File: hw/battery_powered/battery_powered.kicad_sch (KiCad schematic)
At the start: 11 parts, among them SW101 SKRPABE010, SW102 SKRPABE010, U101 RP2040, U102 OSL10564-IB, U103 chofutech_logo

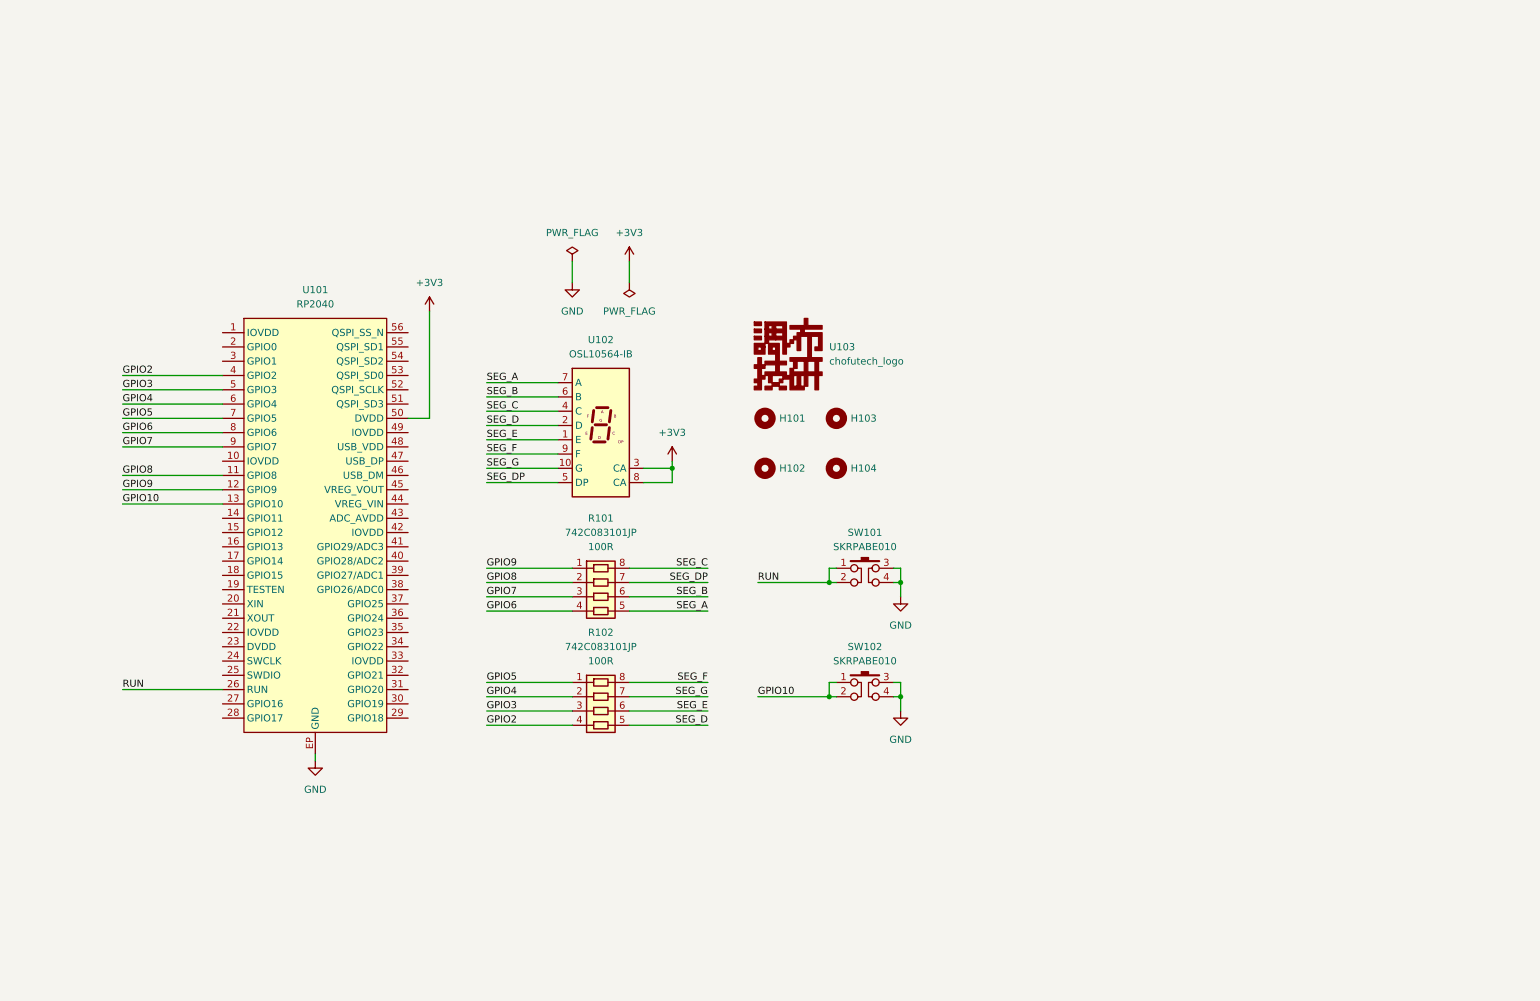
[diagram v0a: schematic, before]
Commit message: filled battery_powered schematics
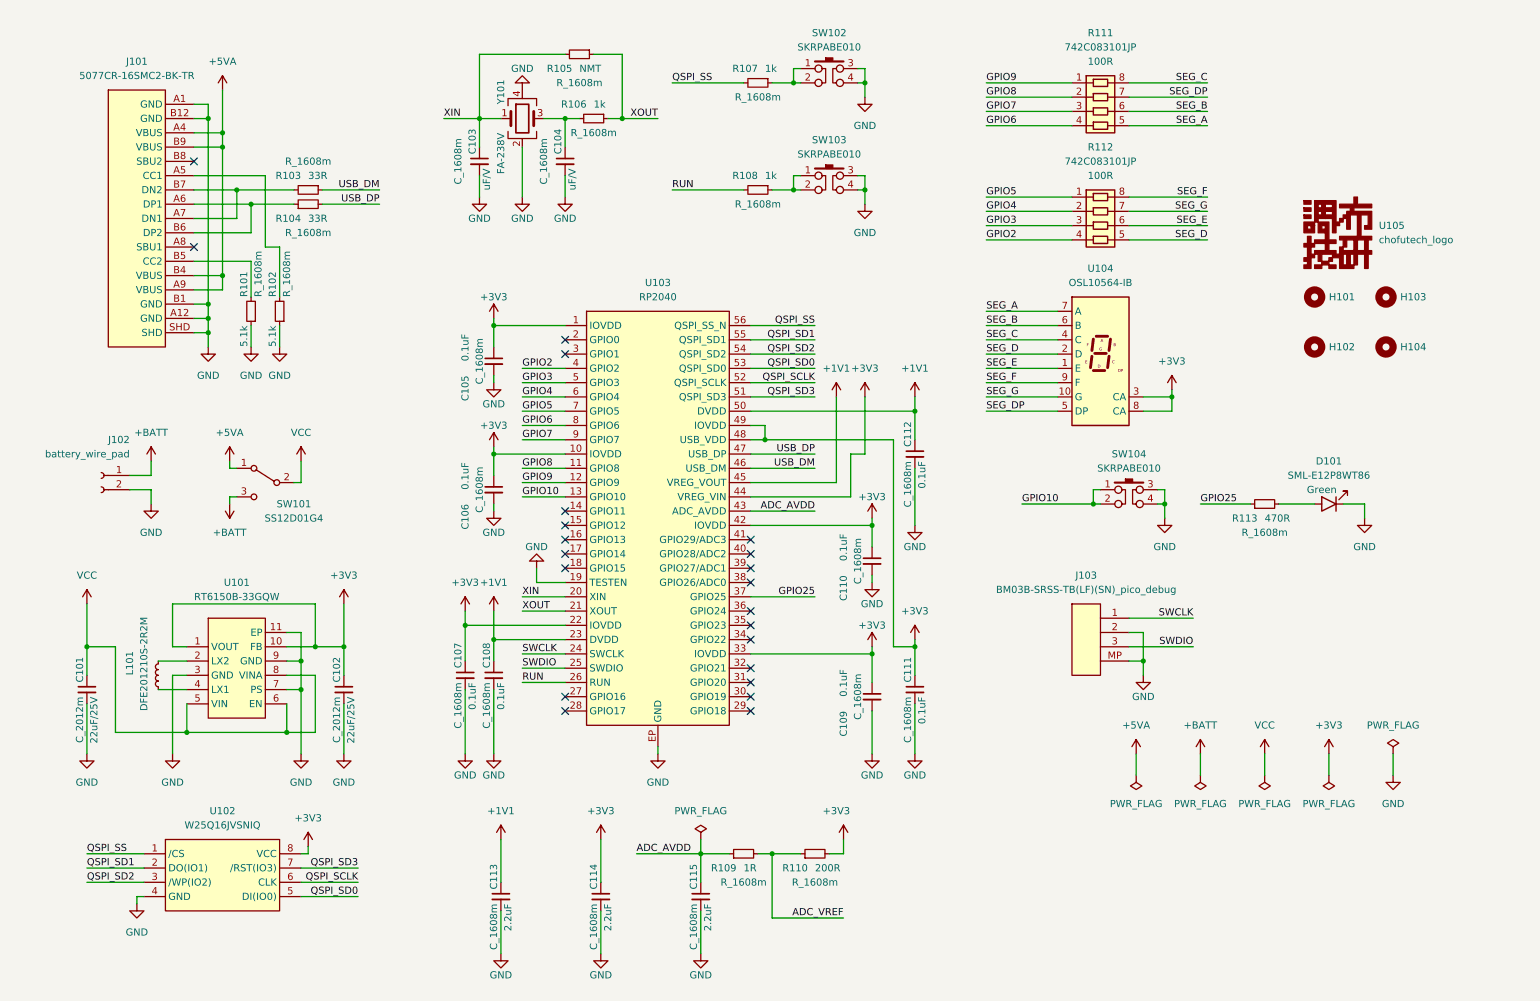
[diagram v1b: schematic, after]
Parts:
- added C101, C102: C_2012m, symbol 00_custom_lib:C_2012m
- added C103, C104, C105, C106, C107, C108, C109, C110, C111, C112, C113, C114, C115: C_1608m, symbol 00_custom_lib:C_1608m
- added D101: SML-E12P8WT86, symbol 00_custom_lib:SML-E12P8WT86
- added J101: 5077CR-16SMC2-BK-TR, symbol 00_custom_lib:5077CR-16SMC2-BK-TR
- added J102: battery_wire_pad, symbol 00_custom_lib:battery_wire_pad
- added J103: BM03B-SRSS-TB(LF)(SN)_pico_debug, symbol 00_custom_lib:BM03B-SRSS-TB(LF)(SN)_pico_debug
- added L101: DFE201210S-2R2M, symbol 00_custom_lib:DFE201210S-2R2M
- added R101, R102, R103, R104, R105, R106, R107, R108, R109, R110, R113: R_1608m, symbol 00_custom_lib:R_1608m
- added SW101: SS12D01G4, symbol 00_custom_lib:SS12D01G4
- added SW102: SKRPABE010, 00_custom_lib:SKRPABE010, symbol 00_custom_lib:SKRPABE010
- added U101: RT6150B-33GQW, symbol 00_custom_lib:RT6150B-33GQW
- added U102: W25Q16JVSNIQ, symbol 00_custom_lib:W25Q16JVSNIQ
- added Y101: FA-238V, symbol 00_custom_lib:FA-238V
- renumbered R101 to R111, R102 to R112, SW101 to SW103, SW102 to SW104, U101 to U103, U102 to U104, U103 to U105
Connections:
- net +3V3: now also U103.1 (IOVDD), U103.10 (IOVDD), U103.22 (IOVDD), U103.33 (IOVDD), U103.42 (IOVDD), U103.44 (VREG_VIN), U103.48 (USB_VDD), U103.49 (IOVDD), C102.1, C105.1, C106.1, C107.1, C109.1, C110.1, C111.1, C114.1, R110.2, U101.1 (VOUT), U101.10 (FB), U102.8 (VCC); no longer U103.50 (DVDD)
- net GND: now also U103.19 (TESTEN), C101.2, C102.2, C103.2, C104.2, C105.2, C106.2, C107.2, C108.2, C109.2, C110.2, C111.2, C112.2, C113.2, C114.2, C115.2, D101.1 (K), J101.A1 (GND), J101.A12 (GND), J101.B1 (GND), J101.B12 (GND), J101.SHD, J102.2 (Pin_2), J103.2, J103.MP, R101.1, R102.1, SW102.3, SW102.4, U101.11 (EP), U101.3 (GND), U101.7 (PS), U101.9 (GND), U102.4 (GND), Y101.2, Y101.4
- net RUN: now also R108.2; no longer SW103.1, SW103.2
- net XIN: now reaches U103.20 (XIN)
- net XIN: now also C103.1, R105.2, Y101.1
- net XOUT: now reaches U103.21 (XOUT)
- net XOUT: now also R105.1, R106.1
- net +1V1: now reaches U103.23 (DVDD)
- net +1V1: now also U103.45 (VREG_VOUT), U103.50 (DVDD), C108.1, C112.1, C113.1
- net SWCLK: now reaches U103.24 (SWCLK)
- net SWCLK: now also J103.1
- net SWDIO: now reaches U103.25 (SWDIO)
- net SWDIO: now also J103.3
- net GPIO25: now reaches U103.37 (GPIO25)
- net GPIO25: now also R113.1
- net ADC_AVDD: now reaches U103.43 (ADC_AVDD)
- net ADC_AVDD: now also C115.1, R109.1
- net USB_DM: now reaches U103.46 (USB_DM)
- net USB_DM: now also R103.1
- net USB_DP: now reaches U103.47 (USB_DP)
- net USB_DP: now also R104.2
- net QSPI_SD3: now reaches U103.51 (QSPI_SD3)
- net QSPI_SD3: now also U102.7 (/RST(IO3))
- net QSPI_SCLK: now reaches U103.52 (QSPI_SCLK)
- net QSPI_SCLK: now also U102.6 (CLK)
- net QSPI_SD0: now reaches U103.53 (QSPI_SD0)
- net QSPI_SD0: now also U102.5 (DI(IO0))
- net QSPI_SD2: now reaches U103.54 (QSPI_SD2)
- net QSPI_SD2: now also U102.3 (/WP(IO2))
- net QSPI_SD1: now reaches U103.55 (QSPI_SD1)
- net QSPI_SD1: now also U102.2 (DO(IO1))
- net QSPI_SS: now reaches U103.56 (QSPI_SS_N)
- net QSPI_SS: now also R107.2, U102.1 (/CS)
- new net: J101.B5 (CC2), R101.2
- new net: L101.1, U101.2 (LX2)
- new net: L101.2, U101.4 (LX1)
- new net: J101.A6 (DP1), J101.B6 (DP2), R104.1
- new net: C104.1, R106.2, Y101.3
- new net: J101.A5 (CC1), R102.2
- new net: R107.1, SW102.1, SW102.2
- new net: J101.A7 (DN1), J101.B7 (DN2), R103.2
- new net: R108.1, SW103.1, SW103.2
- new net: D101.2 (A), R113.2
- new net +5VA: J101.A4 (VBUS), J101.A9 (VBUS), J101.B4 (VBUS), J101.B9 (VBUS), SW101.1 (A)
- new net +BATT: J102.1 (Pin_1), SW101.3 (C)
- new net ADC_VREF: R109.2, R110.1
- new net VCC: C101.1, SW101.2 (B), U101.5 (VIN), U101.6 (EN), U101.8 (VINA)
- no-connect marks 0 -> 22
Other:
- moved on the sheet: H101, H102, H103, H104, R111, R112, SW103, SW104, U103, U104, U105

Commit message: add battery_powered footprints
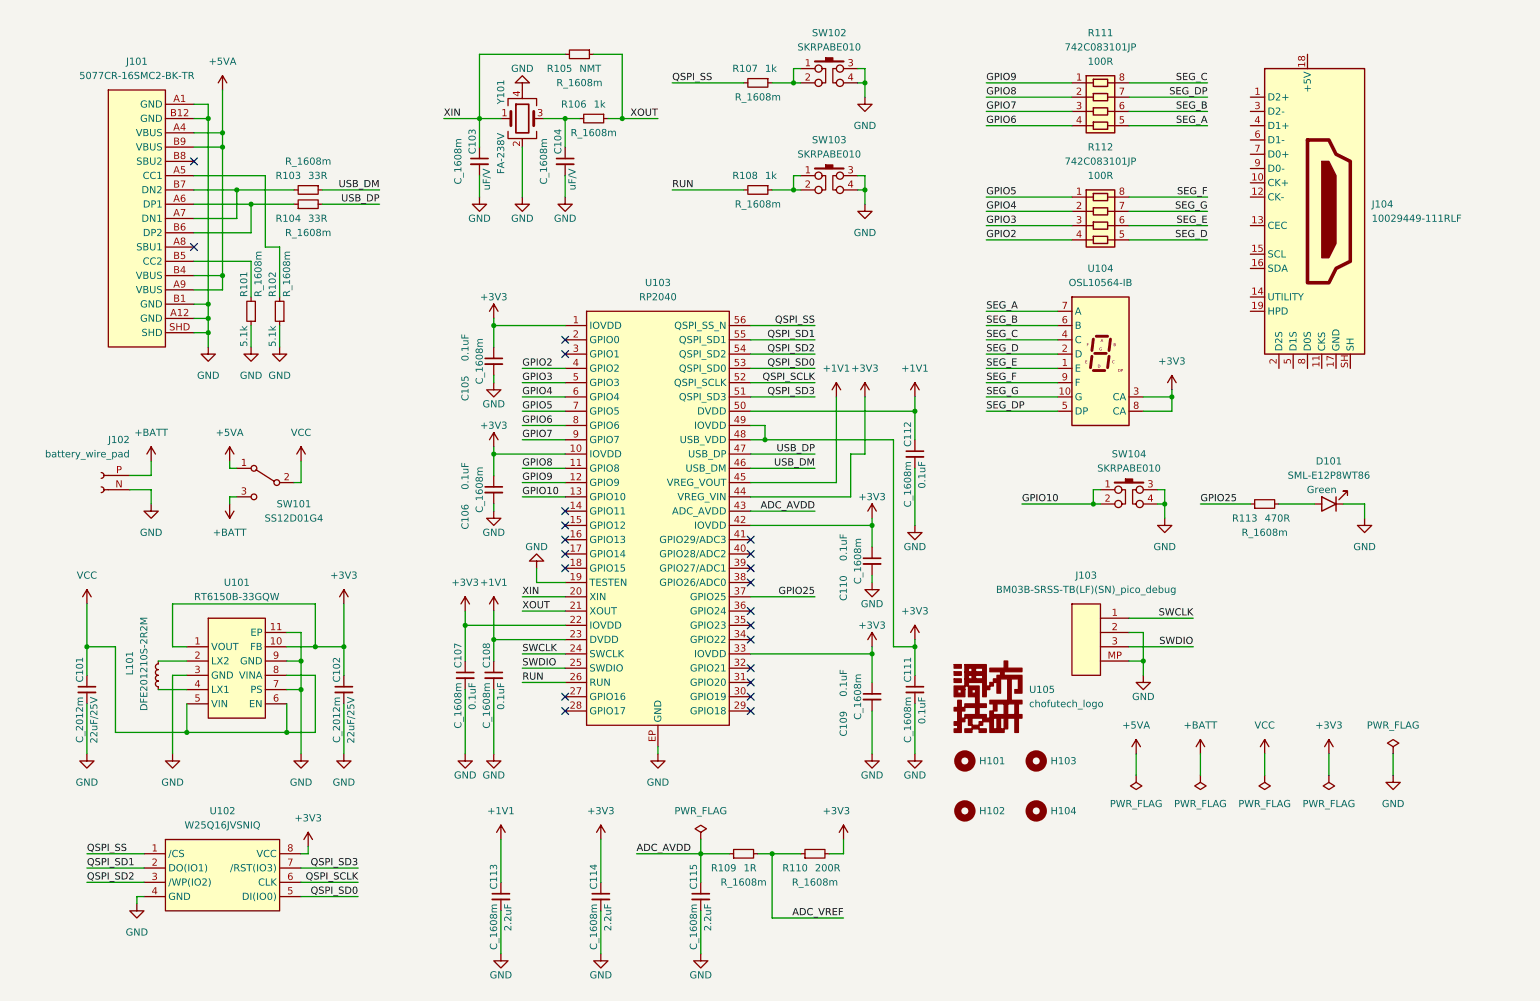
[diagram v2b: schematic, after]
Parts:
- added J104: 10029449-111RLF, 00_custom_lib:10029449-111RLF_hand, symbol 00_custom_lib:10029449-111RLF
- C101, C102: footprint (none) -> 00_custom_lib:C_2012m
- C103, C104, C105, C106, C107, C108, C109, C110, C111, C112, C113, C114, C115: footprint (none) -> 00_custom_lib:C_1608m
- D101: footprint (none) -> 00_custom_lib:SML-E12P8WT86
- J101: footprint (none) -> 00_custom_lib:5077CR-16SMC2-BK-TR_hand
- J102: footprint (none) -> 00_custom_lib:battery_wire_pad
- J103: footprint (none) -> 00_custom_lib:BM03B-SRSS-TB(LF)(SN)_hand
- L101: footprint (none) -> 00_custom_lib:DFE201210S-2R2M
- R101, R102, R103, R104, R105, R106, R107, R108, R109, R110, R113: footprint (none) -> 00_custom_lib:R_1608m
- SW101: footprint (none) -> 00_custom_lib:SS12D01G4
- U101: footprint (none) -> 00_custom_lib:RT6150B-33GQW
- U102: footprint (none) -> 00_custom_lib:W25Q16JVSNIQ
- U103: footprint (none) -> 00_custom_lib:RP2040
- Y101: footprint (none) -> 00_custom_lib:FA-238V
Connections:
- net +BATT: now also J102.P (Pin_1); no longer J102.1 (Pin_1)
- net GND: now also J102.N (Pin_2); no longer J102.2 (Pin_2)
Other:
- moved on the sheet: H101, H102, H103, H104, U105

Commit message: add DVI output circuit to battery_powered composition
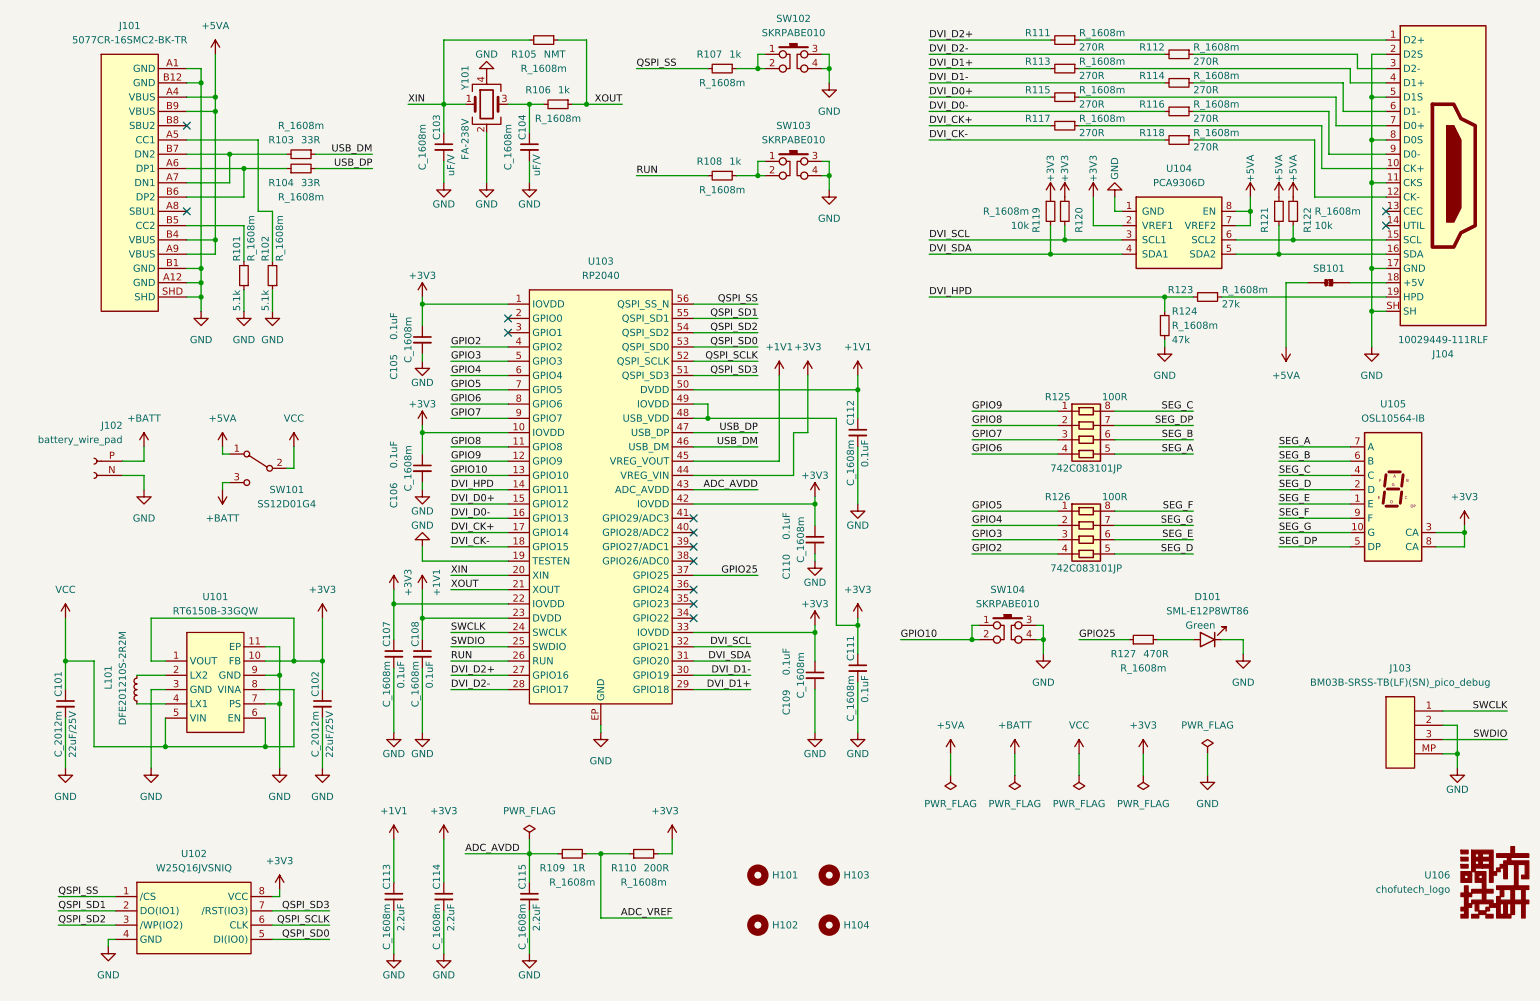
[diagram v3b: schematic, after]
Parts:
- added R111, R112, R113, R114, R115, R116, R117, R118, R119, R120, R121, R122, R123, R124: R_1608m, 00_custom_lib:R_1608m, symbol 00_custom_lib:R_1608m
- added SB101: jumper_2pole_solder, 00_custom_lib:jumper_2pole_solder, symbol 00_custom_lib:jumper_2pole_solder
- added U104: PCA9306D, 00_custom_lib:PCA9306D, symbol 00_custom_lib:PCA9306D
- SW102, SW103, SW104: footprint 00_custom_lib:SKRPABE010 -> 00_custom_lib:SKRPABE010_hand
- renumbered R111 to R125, R112 to R126, R113 to R127, U104 to U105, U105 to U106
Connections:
- net +3V3: now also R119.1, R120.1, U104.2 (VREF1)
- net +5VA: now also R121.1, R122.1, SB101.1 (A), U104.7 (VREF2), U104.8 (EN)
- net GND: now also J104.11 (CKS), J104.17 (GND), J104.2 (D2S), J104.5 (D1S), J104.8 (D0S), J104.SH, R124.2, U104.1 (GND)
- net DVI_HPD: now reaches U103.14 (GPIO11)
- net DVI_HPD: now also R123.2, R124.1
- net DVI_D0+: now reaches U103.15 (GPIO12)
- net DVI_D0+: now also R115.2
- net DVI_D0-: now reaches U103.16 (GPIO13)
- net DVI_D0-: now also R116.2
- net DVI_CK+: now reaches U103.17 (GPIO14)
- net DVI_CK+: now also R117.2
- net DVI_CK-: now reaches U103.18 (GPIO15)
- net DVI_CK-: now also R118.2
- net DVI_D2+: now reaches U103.27 (GPIO16)
- net DVI_D2+: now also R111.2
- net DVI_D2-: now reaches U103.28 (GPIO17)
- net DVI_D2-: now also R112.2
- net DVI_D1+: now reaches U103.29 (GPIO18)
- net DVI_D1+: now also R113.2
- net DVI_D1-: now reaches U103.30 (GPIO19)
- net DVI_D1-: now also R114.2
- net DVI_SDA: now reaches U103.31 (GPIO20)
- net DVI_SDA: now also R119.2, U104.4 (SDA1)
- net DVI_SCL: now reaches U103.32 (GPIO21)
- net DVI_SCL: now also R120.2, U104.3 (SCL1)
- net at J104.1 (D2+): now also R111.1
- net at J104.10 (CK+): now also R117.1
- net at J104.12 (CK-): now also R118.1
- net at J104.15 (SCL): now also R122.2, U104.6 (SCL2)
- net at J104.16 (SDA): now also R121.2, U104.5 (SDA2)
- net at J104.18 (+5V): now also SB101.2 (B)
- net at J104.19 (HPD): now also R123.1
- net at J104.3 (D2-): now also R112.1
- net at J104.4 (D1+): now also R113.1
- net at J104.6 (D1-): now also R114.1
- net at J104.7 (D0+): now also R115.1
- net at J104.9 (D0-): now also R116.1
- no-connect marks 22 -> 13
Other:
- moved on the sheet: C101, C102, C103, C104, C105, C106, C107, C108, C109, C110, C111, C112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
